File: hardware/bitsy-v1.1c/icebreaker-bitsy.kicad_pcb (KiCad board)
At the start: 4 copper layers, 36 x 18 mm, 106 parts, among them J1 USB_C, P0 0, P1 1, P10 10, P11 11, P12 12, P13 13, P14 14, P15 15, P16 16, P17 17, P18 18, P19 19, P2 2, P20 20, P21 21, P22 22, P23 23, P24 GND, P25 GND, P26 GND, P27 3V3, P28 3V3, P29 VIN, P3 3, P30 CDONE, P31 CRESET, P32 UP, P33 UP, P34 UP, P35 UP, P36 CS, P37 SCK, P38 CIPO, P39 COPI, P4 4, P40 IO3, P41 IO2, P5 5, P6 6, P7 7, P8 8, P9 9, SW1 TACT, U1 USBLC6-2, U2 TLV75533PDRV, U3 TLV73312PDRV, U4 LY68L6400, U5 W25Q128JVxxM, U6 ICE40UP5K-SG48, X1 12MHz

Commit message: Fixed silkscreen
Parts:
- removed LOGO1: 1BitSquared, pkl_logos:null_Logo_SilkS_2mm
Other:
- board text added: "WWU"
- board text removed: "~{CS}"

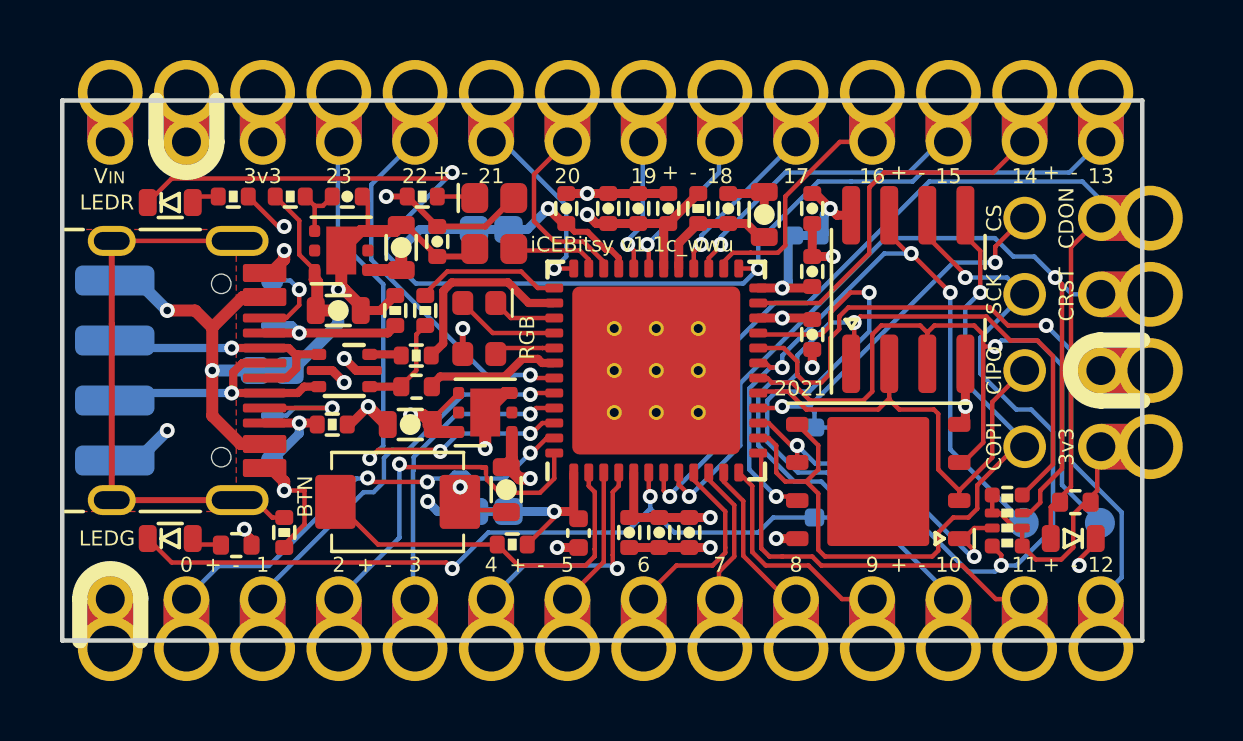
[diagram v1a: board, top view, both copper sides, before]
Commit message: Fixed footprint of U5, etc.
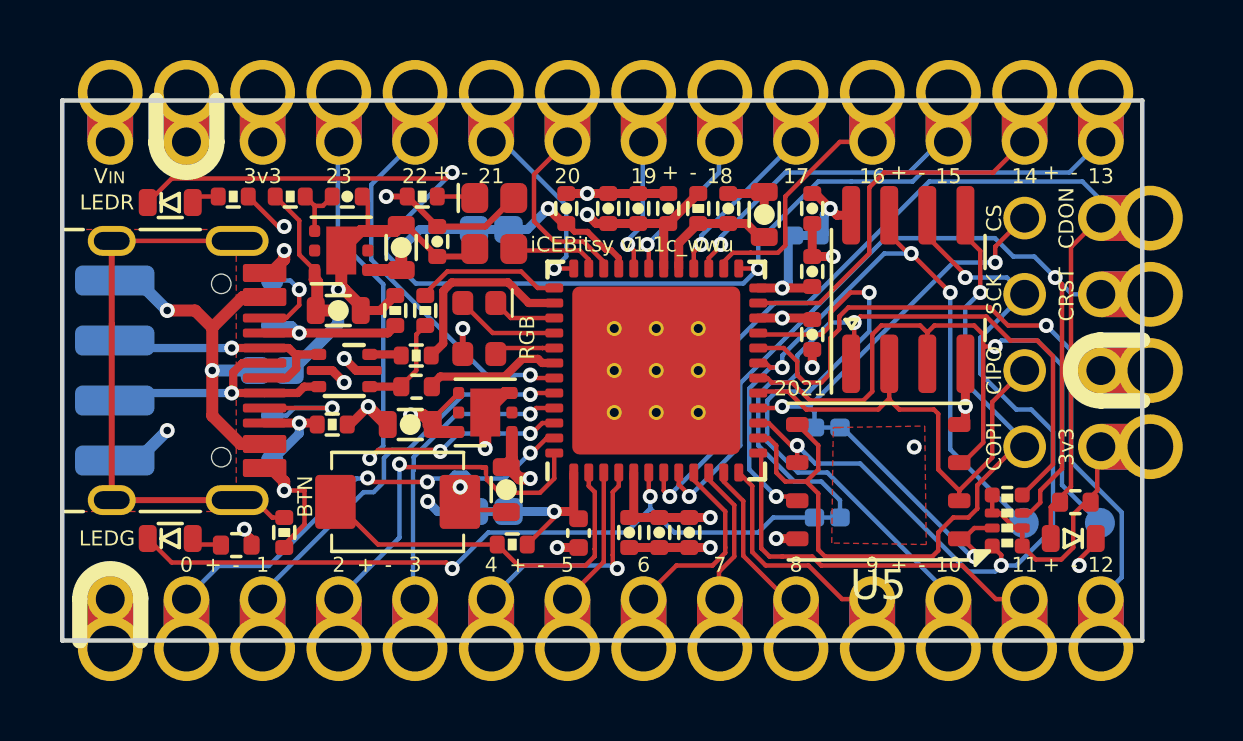
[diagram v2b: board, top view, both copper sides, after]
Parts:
- U5: footprint Package_SON:WSON-8-1EP_6x5mm_P1.27mm_EP3.4x4.3mm -> WSON-Library:WSON-8-1EP_6x5mm_P1.27mm_EP3.4x4.3mm
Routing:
- net GND: vias 16 -> 17
- added copper zone on F.Cu, net GND
